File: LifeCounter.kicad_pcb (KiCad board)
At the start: 2 copper layers, 132.3 x 43.9 mm, 11 parts, among them IC1 STM32H562RGT6, J1 54104-4531

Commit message: finished the power circuit for the LCD backlight
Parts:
- added C1: CL21B105KBFNNNE, LifeCounter-Footprints:Samsung_CAPC2012X135M, F.Cu at (175.2, 71.0)
- added C2: CL21B105KBFNNNE, LifeCounter-Footprints:Samsung_CAPC2012X135M, F.Cu at (158.2, 66.2)
- added C3: CL21B105KBFNNNE, LifeCounter-Footprints:Samsung_CAPC2012X135M, F.Cu at (158.2, 69.2)
- added D1: 1N5819HWQ-7-F, LifeCounter-Footprints:Diodes-Inc_SOD3716X145M, F.Cu at (165.0, 65.8)
- added IC2: AP3012KTR-E1, LifeCounter-Footprints:Diodes-Inc_SOT95P282X145-5M, F.Cu at (170.2, 71.8)
- added L1: VLS3012CX-100M-1, LifeCounter-Footprints:TDK_VLS3012, F.Cu at (171.0, 66.0)
- added R1: 0805S8F820JT5E, Resistor_SMD:R_0805_2012Metric_Pad1.20x1.40mm_HandSolder, F.Cu at (164.5, 73.2)
- moved IC1 3.01 mm to (172.2, 86.2)
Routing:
- net Net-(IC2-GND): track 0.00 -> 20.6 mm
- net Net-(D1-K): track 0.00 -> 9.52 mm
- net Net-(IC2-VIN): track 0.00 -> 8.98 mm
- net Net-(D1-A): track 0.00 -> 8.52 mm
- net Net-(IC2-FB): track 0.00 -> 5.09 mm

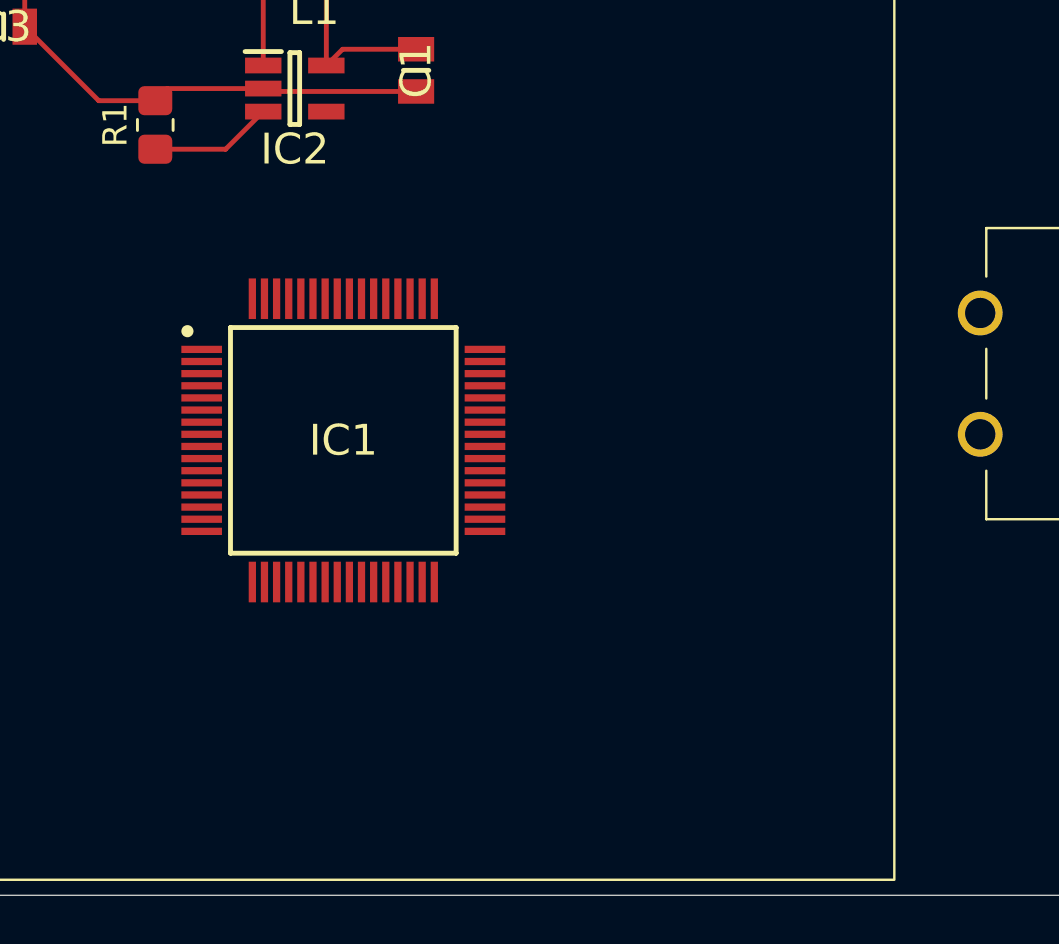
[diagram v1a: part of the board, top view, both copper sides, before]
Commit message: bump version to v0.0.3, add USB C and TVS diode
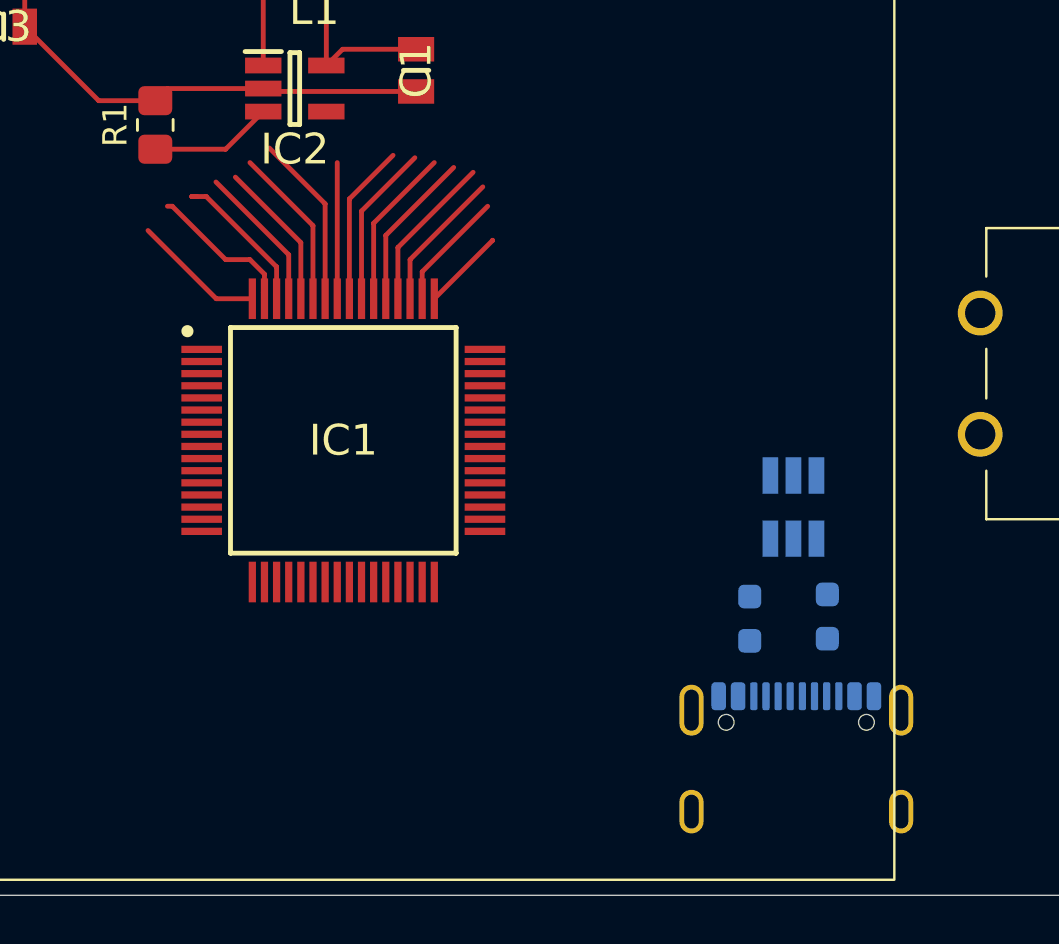
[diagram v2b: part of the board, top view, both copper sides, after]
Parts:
- added D2: ESDA25SC6Y, LifeCounter-Footprints:STMicroelectronics_SOT95P280X145-6M, B.Cu at (190.8, 89.0)
- added J2: USB_C_Receptacle_USB2.0_14P, Connector_USB:USB_C_Receptacle_GCT_USB4105-xx-A_16P_TopMnt_Horizontal, B.Cu at (190.9, 100.5)
- added R2: 5k1, Resistor_SMD:R_0603_1608Metric_Pad0.98x0.95mm_HandSolder, B.Cu at (189.0, 93.6)
- added R3: 5k1, Resistor_SMD:R_0603_1608Metric_Pad0.98x0.95mm_HandSolder, B.Cu at (192.2, 93.5)
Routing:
- net unconnected-(IC1-PB6-Pad58): track 0.00 -> 7.16 mm
- net unconnected-(IC1-PB3-Pad55): track 0.00 -> 6.72 mm
- net unconnected-(IC1-PB7-Pad59): track 0.00 -> 6.69 mm
- net unconnected-(IC1-PB4-Pad56): track 0.00 -> 6.66 mm
- net unconnected-(IC1-PD2-Pad54): track 0.00 -> 6.65 mm
- net unconnected-(IC1-PC12-Pad53): track 0.00 -> 6.57 mm
- net unconnected-(IC1-PC11-Pad52): track 0.00 -> 6.50 mm
- net unconnected-(IC1-VSS_4-Pad63): track 0.00 -> 6.45 mm
- net unconnected-(IC1-VCAP_2-Pad62): track 0.00 -> 6.21 mm
- net unconnected-(IC1-BOOT0-Pad60): track 0.00 -> 6.13 mm
- net unconnected-(IC1-PB8-Pad61): track 0.00 -> 6.05 mm
- net unconnected-(IC1-PC10-Pad51): track 0.00 -> 5.85 mm
- net unconnected-(IC1-PB5-Pad57): track 0.00 -> 5.61 mm
- net unconnected-(IC1-VDD_4-Pad64): track 0.00 -> 5.46 mm
- net unconnected-(IC1-PA15-Pad50): track 0.00 -> 4.93 mm
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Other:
- copper layers 2 -> 4

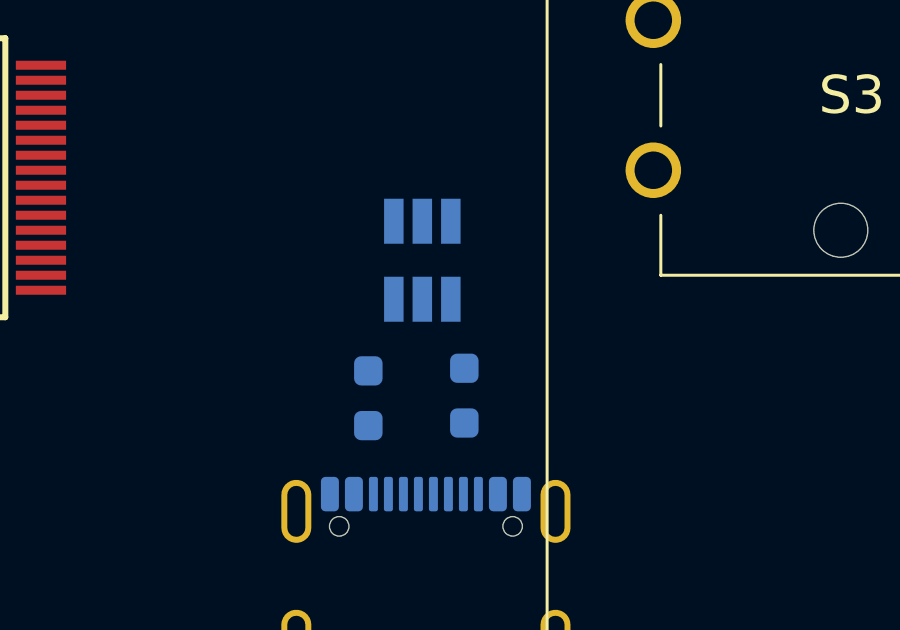
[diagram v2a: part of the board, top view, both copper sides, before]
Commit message: added a 10uF 0603 capacitor for usb c VBUS
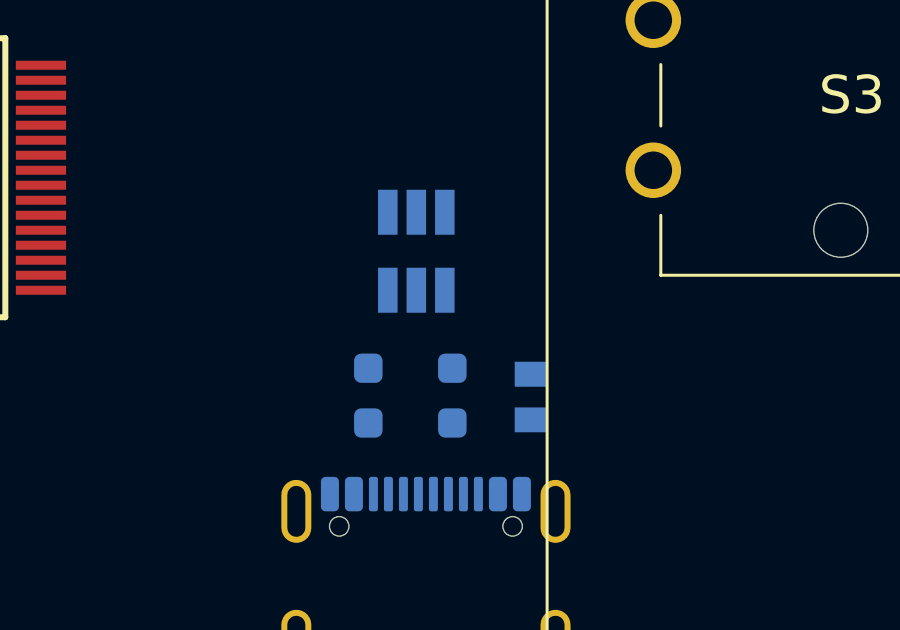
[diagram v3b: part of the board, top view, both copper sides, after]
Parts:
- added C4: CL10A106KP8NNNC, LifeCounter-Footprints:Samsung_CAPC1608X90M, B.Cu at (194.4, 93.6)
- moved R3 0.40 mm to (191.8, 93.5)
- moved D2 0.36 mm to (190.6, 88.7)
- moved R2 0.09 mm to (189.0, 93.5)
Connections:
- J2 pad A1: Net-(J2-GND-PadA1) -> GND
- J2 pad A12: Net-(J2-GND-PadA1) -> GND
- J2 pad B1: Net-(J2-GND-PadA1) -> GND
- J2 pad B12: Net-(J2-GND-PadA1) -> GND
- J2 pad S1: unconnected-(J2-SHIELD-PadS1) -> GND

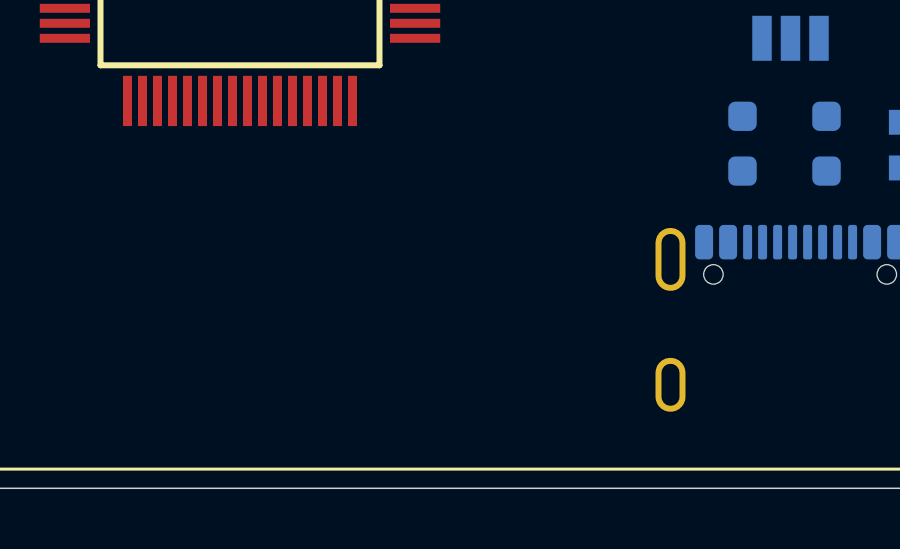
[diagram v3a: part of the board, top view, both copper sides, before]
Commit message: added lipo charger and red led indicator diode
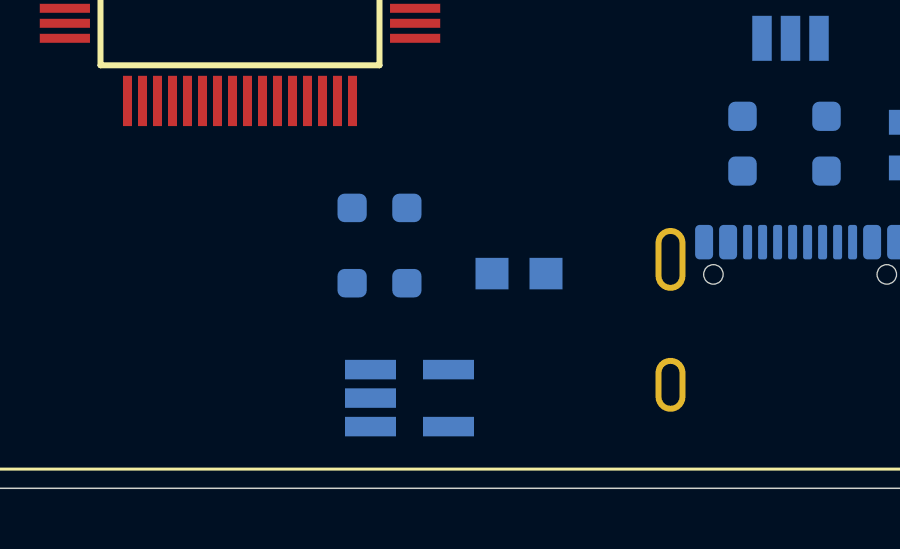
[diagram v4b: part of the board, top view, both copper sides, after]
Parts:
- added IC3: MCP73831T-2ATI_OT, LifeCounter-Footprints:Microchip_SOT95P270X145-5M, B.Cu at (177.9, 102.0)
- added LED1: LTST-C191KRKT, LifeCounter-Footprints:Liteon_LEDC1608X55M, B.Cu at (181.6, 97.8)
- added R4: 2k, Resistor_SMD:R_0603_1608Metric_Pad0.98x0.95mm_HandSolder, B.Cu at (176.9, 98.2)
- added R5: 470, Resistor_SMD:R_0603_1608Metric_Pad0.98x0.95mm_HandSolder, B.Cu at (176.9, 95.7)
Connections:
- D2 pad 3: /DN+ -> /DN
- D2 pad 6: /DN- -> /DP
- IC1 pad 44: unconnected-(IC1-PA11-Pad44) -> /DN
- IC1 pad 45: unconnected-(IC1-PA12-Pad45) -> /DP
- J2 pad A6: /DN+ -> /DP
- J2 pad A7: /DN- -> /DN
- J2 pad B6: /DN+ -> /DP
- J2 pad B7: /DN- -> /DN

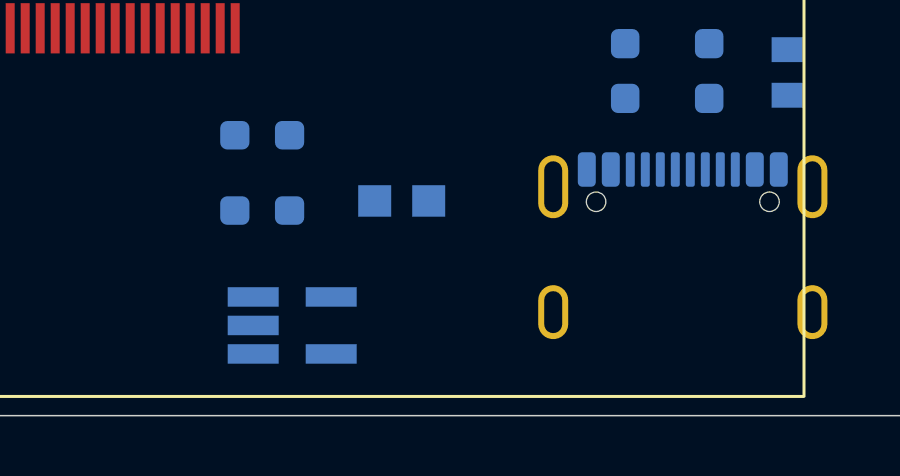
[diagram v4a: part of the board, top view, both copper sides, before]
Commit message: added 4.7uF capacitors for the lipo charger
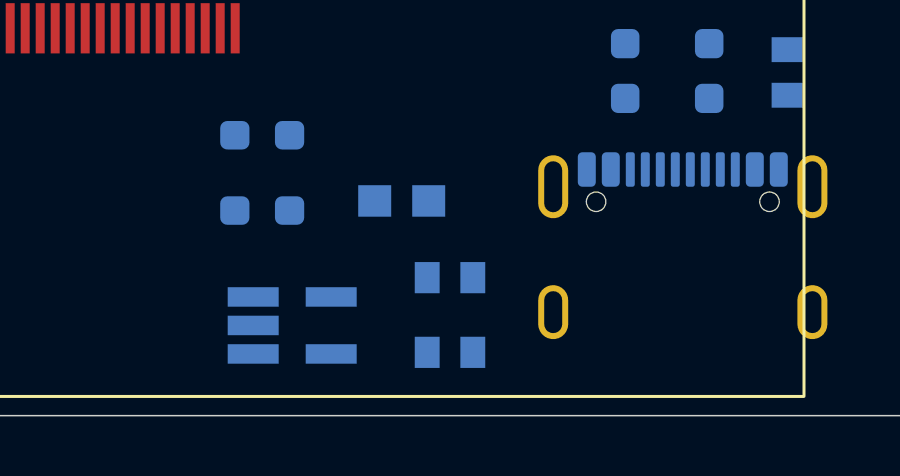
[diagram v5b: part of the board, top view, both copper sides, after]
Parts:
- added C5: CL10A475KP8NNNC, LifeCounter-Footprints:Samsung_CAPC1608X90M, B.Cu at (183.2, 102.9)
- added C6: CL10A475KP8NNNC, LifeCounter-Footprints:Samsung_CAPC1608X90M, B.Cu at (183.2, 100.4)
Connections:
- IC3 pad 3: unconnected-(IC3-VBAT-Pad3) -> Net-(BT1-+)

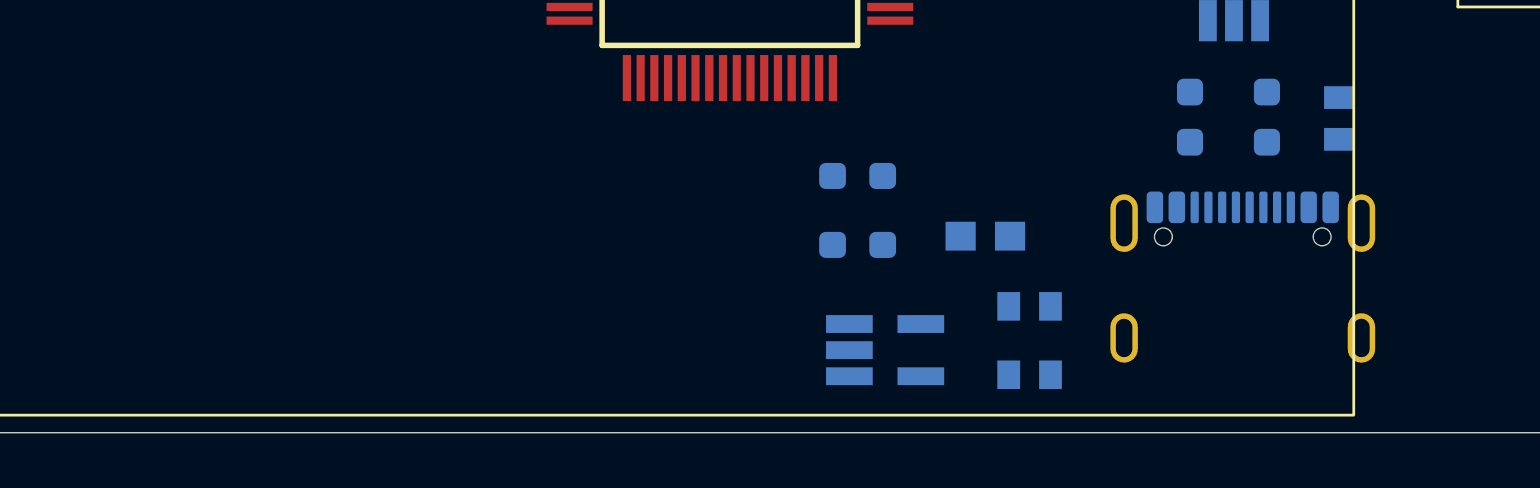
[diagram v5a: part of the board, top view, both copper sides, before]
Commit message: added LDO for 3v3 power delivery and a 100nF capacitor
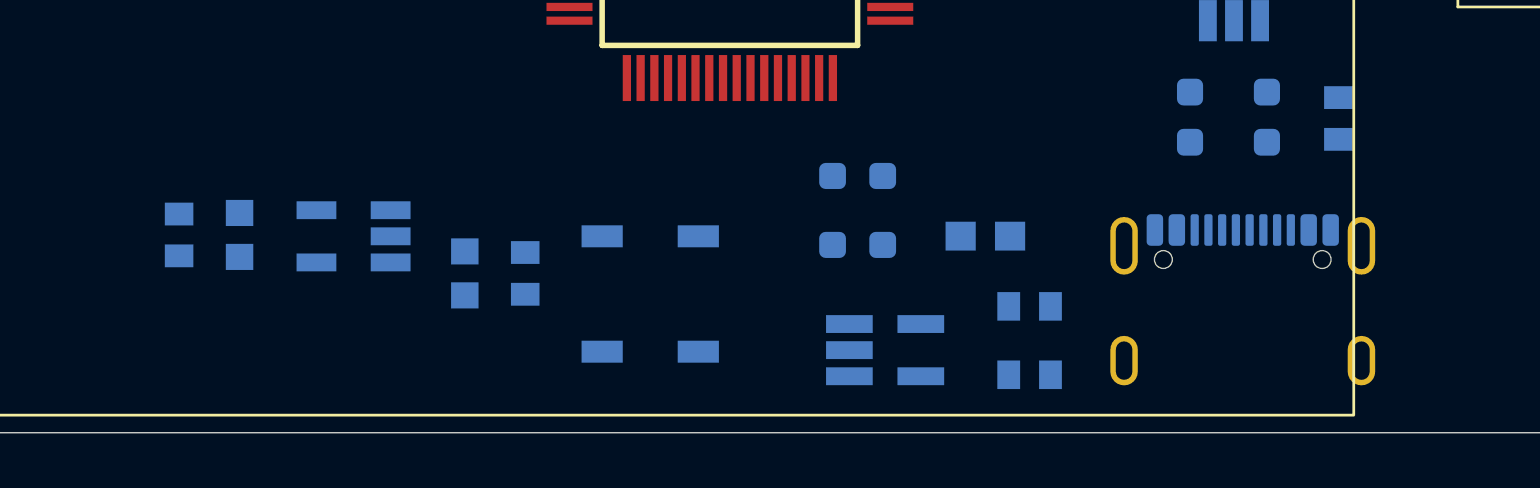
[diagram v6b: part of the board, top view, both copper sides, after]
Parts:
- added C10: C0603C104K8RACTU, LifeCounter-Footprints:Kemet_C0603, B.Cu at (154.4, 97.8)
- added C7: CL10A106KP8NNNC, LifeCounter-Footprints:Samsung_CAPC1608X90M, B.Cu at (164.8, 99.2)
- added C8: C0603C104K8RACTU, LifeCounter-Footprints:Kemet_C0603, B.Cu at (162.6, 99.2)
- added C9: CL10A106KP8NNNC, LifeCounter-Footprints:Samsung_CAPC1608X90M, B.Cu at (152.2, 97.8)
- added D3: 1N5819HWQ-7-F, LifeCounter-Footprints:Diodes-Inc_SOD3716X145M, B.Cu at (169.3, 102.0)
- added D4: 1N5819HWQ-7-F, LifeCounter-Footprints:Diodes-Inc_SOD3716X145M, B.Cu at (169.3, 97.8)
- added IC4: AP2112K-3.3TRG1, LifeCounter-Footprints:Diodes_Inc-SOT95P285X140-5M, B.Cu at (158.6, 97.8)
- moved J2 0.83 mm to (190.9, 101.3)
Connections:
- C5 pad 1: Net-(IC3-VDD) -> /VBUS
- IC1 pad 1: unconnected-(IC1-VBAT-Pad1) -> +3V3
- IC1 pad 12: unconnected-(IC1-VSSA-Pad12) -> GND
- IC1 pad 13: unconnected-(IC1-VDDA-Pad13) -> +3V3
- IC1 pad 18: unconnected-(IC1-VSS_1-Pad18) -> GND
- IC1 pad 19: unconnected-(IC1-VDD_1-Pad19) -> +3V3
- IC1 pad 31: unconnected-(IC1-VSS_2-Pad31) -> GND
- IC1 pad 32: unconnected-(IC1-VDD_2-Pad32) -> +3V3
- IC1 pad 47: unconnected-(IC1-VSS_3-Pad47) -> GND
- IC1 pad 48: unconnected-(IC1-VDD_3-Pad48) -> +3V3
- IC1 pad 63: unconnected-(IC1-VSS_4-Pad63) -> GND
- IC1 pad 64: unconnected-(IC1-VDD_4-Pad64) -> +3V3
- IC3 pad 4: Net-(IC3-VDD) -> /VBUS
- LED1 pad 2: Net-(IC3-VDD) -> /VBUS
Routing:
- net unconnected-(IC1-VSS_4-Pad63): track 6.45 -> 0.00 mm
- net GND: track 0.00 -> 6.45 mm
- net unconnected-(IC1-VDD_4-Pad64): track 5.46 -> 0.00 mm
- net +3V3: track 0.00 -> 5.46 mm
